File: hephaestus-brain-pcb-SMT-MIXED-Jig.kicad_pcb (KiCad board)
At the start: 2 copper layers, 80 x 60 mm, 34 parts, among them J1 Conn_01x19_Female, J2 Conn_01x19_Female, J3 Barrel_Jack, J4 Conn_01x11_Female, SW1 SW_Push

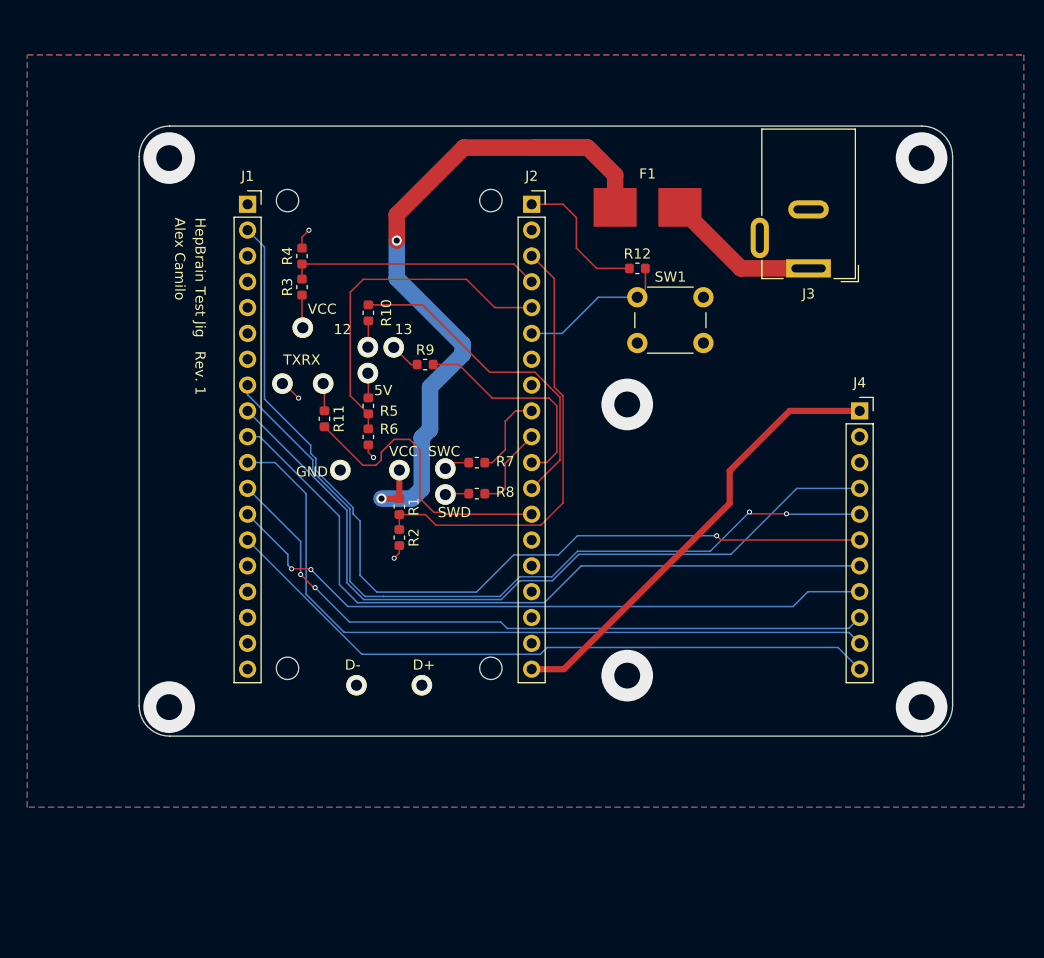
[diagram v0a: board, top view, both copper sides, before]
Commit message: finished jig pcb
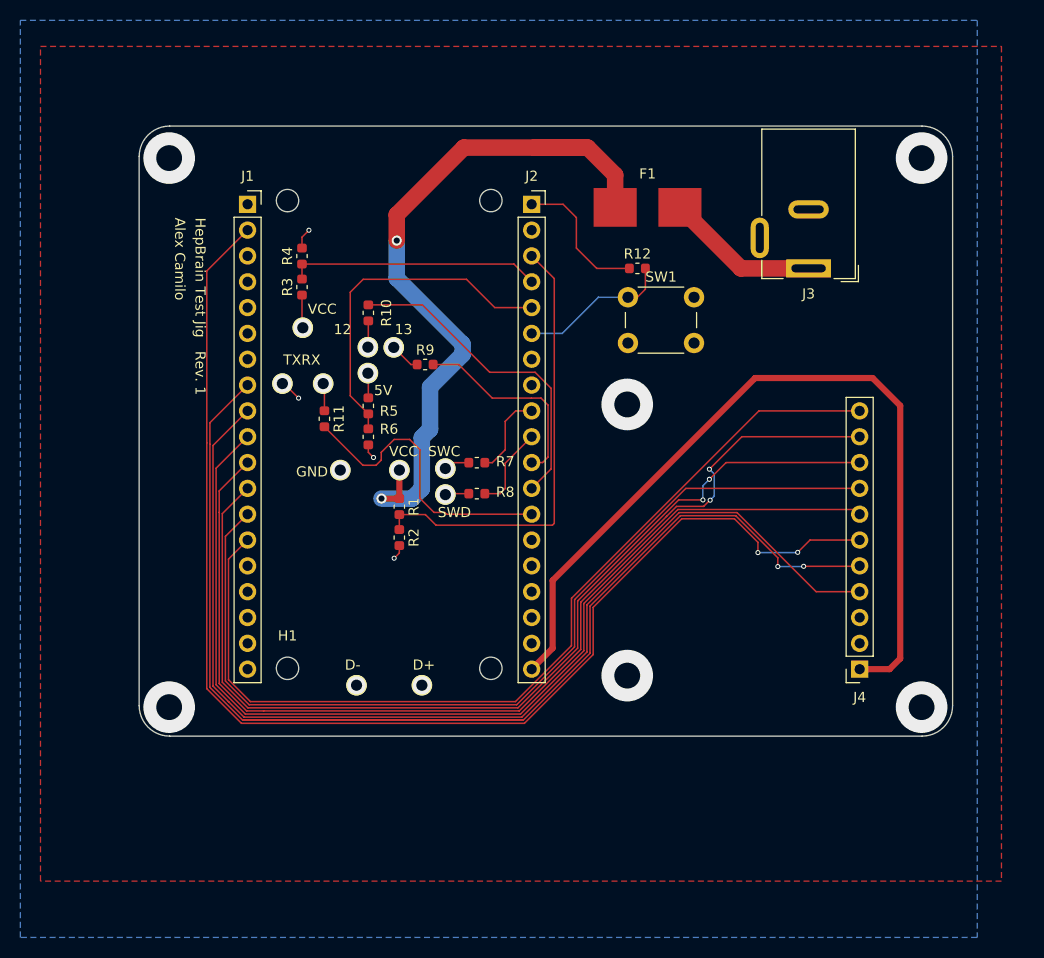
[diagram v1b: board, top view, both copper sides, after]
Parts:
- moved J4 25.4 mm to (200.9, 108.4), turned to 180 degrees
- moved SW1 0.92 mm to (178.1, 71.8)
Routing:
- net MISO: track 77.8 -> 137.7 mm
- net +5V: track 44.7 -> 82.4 mm
- net MOSI: track 90.8 -> 125.9 mm, vias 1 -> 2
- net SCK: track 76.6 -> 107.6 mm
- net SSSD: track 73.4 -> 103.1 mm, vias 0 -> 2
- net DC: track 68.3 -> 97.4 mm
- net SSTFT: track 72.4 -> 101.4 mm
- net RST: track 65.2 -> 92.2 mm, vias 2 -> 0
- net LIT: track 66.0 -> 92.0 mm
- net Net-(J2-Pad11): track 21.3 -> 19.9 mm
- net Net-(J2-Pad12): track 32.7 -> 32.0 mm
